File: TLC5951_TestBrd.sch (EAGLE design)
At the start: 7 parts, among them U1 V_REG_317SMD

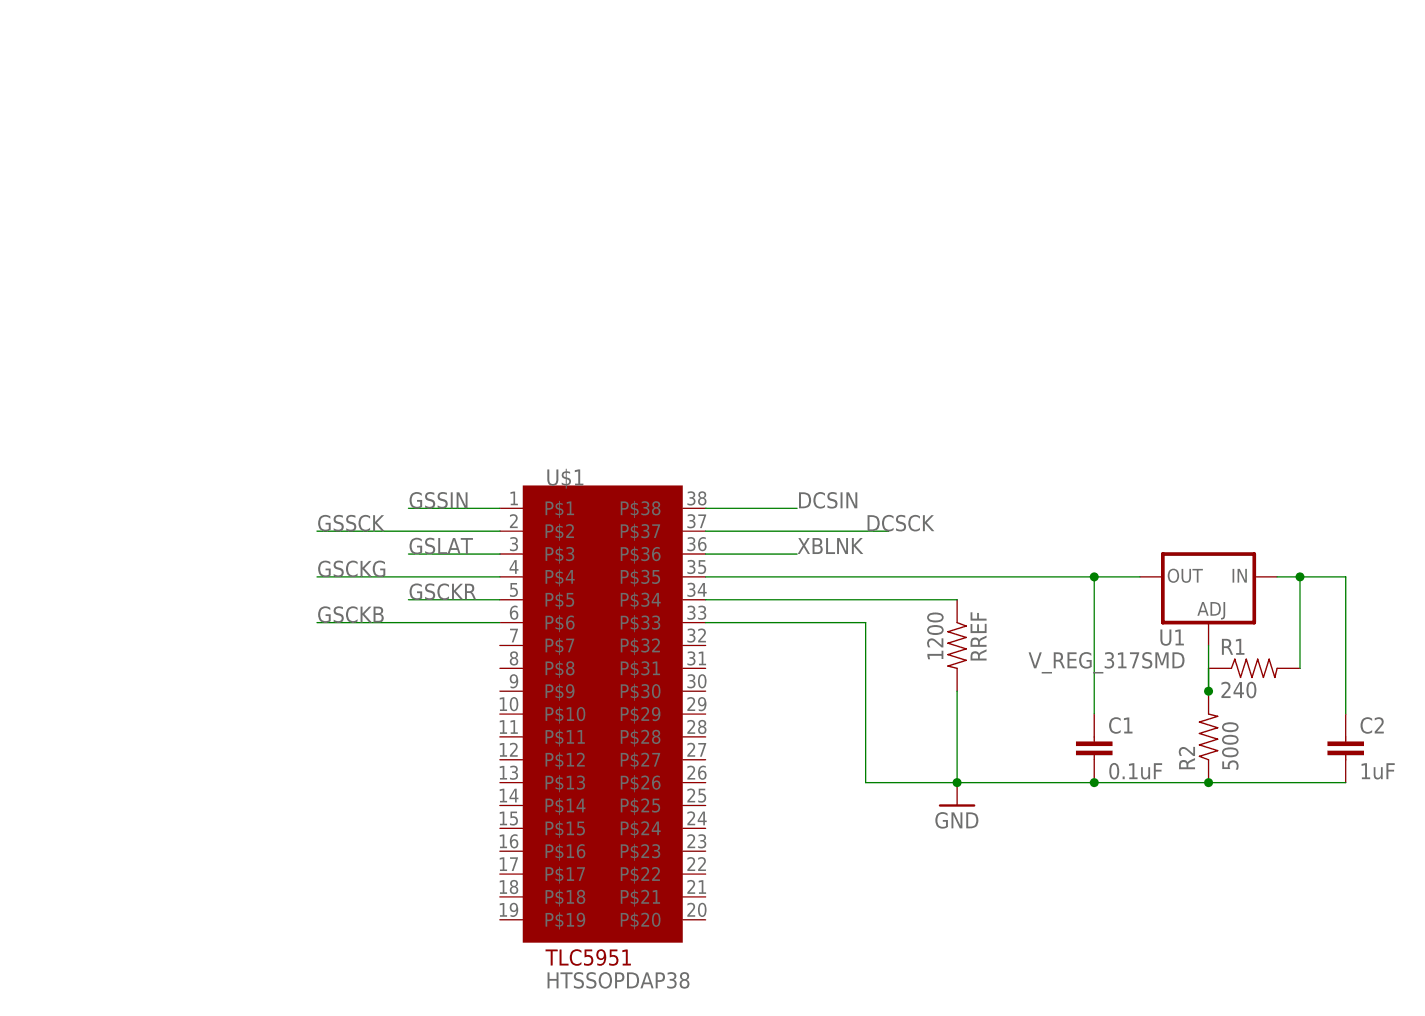
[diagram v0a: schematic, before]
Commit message: added new LDO Voltage Regulator
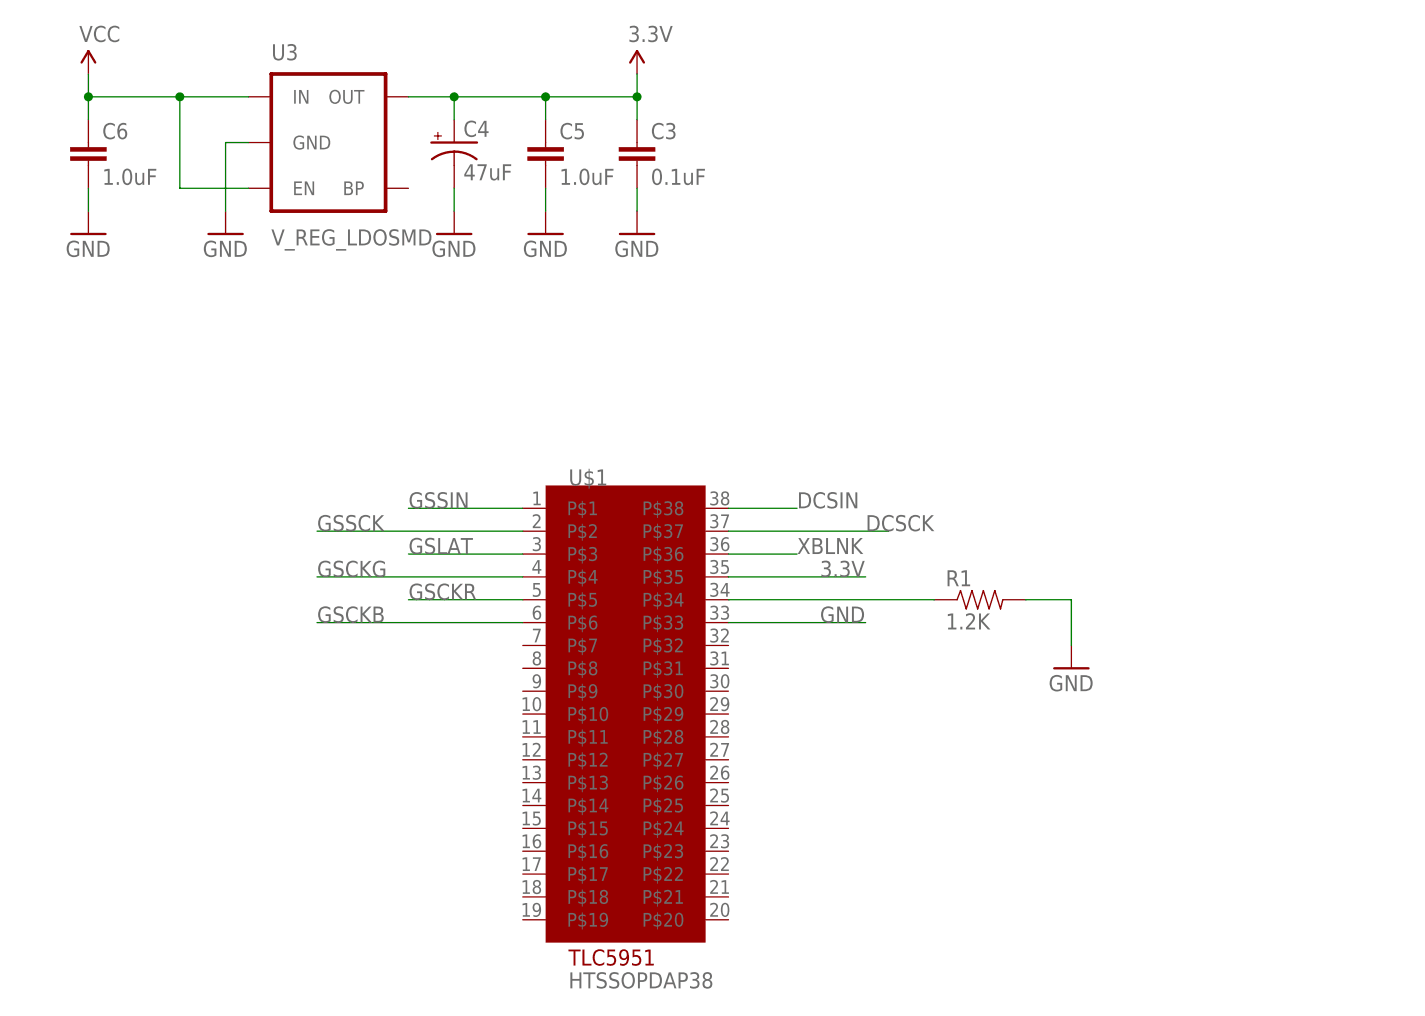
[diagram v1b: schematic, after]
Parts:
- removed C1: 0.1uF, SparkFun-Passives:CAP1210
- removed C2: 1uF, SparkFun-Passives:CAP1210
- removed R2: 5000, SparkFun-Passives:RESISTOR2512
- removed RREF: 1200, SparkFun-Passives:RESISTOR2512
- removed U1: V_REG_317SMD, SparkFun-PowerIC:V_REG_317SMD
- added C3: 0.1uF, SparkFun:CAP0402-CAP
- added C4: 47uF, SparkFun:CAP_POL3528
- added C5, C6: 1.0uF, SparkFun:CAP0402-CAP
- added U3: V_REG_LDOSMD, SparkFun:V_REG_LDOSMD
- R1: value 240 -> 1.2K; device SparkFun-Passives:RESISTOR2512 -> SparkFun-Passives:RESISTORPTH-1W
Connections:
- removed net N$1: RREF.1, U$1.P$34
- removed net N$3: C2.1, R1.2, U1.IN
- removed net N$4: R1.1, R2.2, U1.ADJ
- new net 3.3V: C3.1, C4.+, C5.1, U$1.P$35, U3.OUT
- new net VCC: C6.1, U3.EN, U3.IN
- net GND: now also C3.2, C4.-, C5.2, C6.2, R1.2, U3.GND; no longer C1.2, C2.2, R2.1, RREF.2
- net N$2: now also R1.1, U$1.P$34; no longer C1.1, U$1.P$35, U1.OUT
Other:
- moved on the sheet: R1, U$1

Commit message: Updated TLC5951 Eagle library and Breakout Board Project File
1. Updated TLC5951_DAP38 Eagle library by removing tsop under the
central section of the chip, and by adding holes.
2. Updated TLC5951_TestBrd schematic by adding headers and using new
DAP38 device details
3. Created TLC5951 layout with passive components and appropriate
traces.
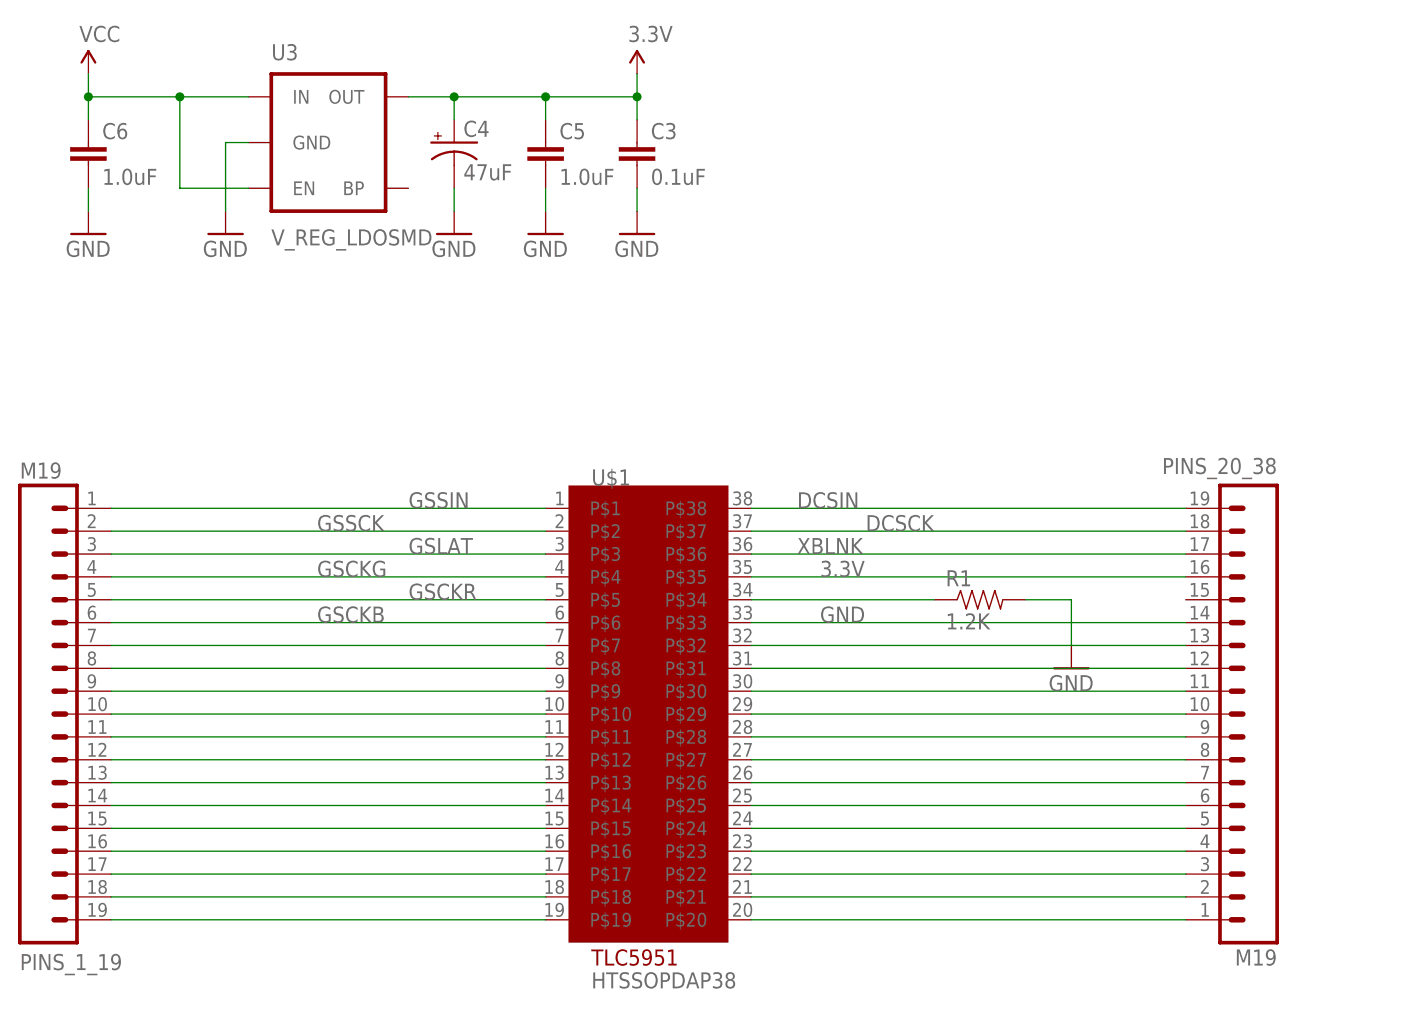
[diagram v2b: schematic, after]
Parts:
- added PINS_1_19, PINS_20_38: M19, SparkFun-Connectors:M19
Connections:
- new net N$1: PINS_20_38.13, U$1.P$32
- new net N$10: PINS_20_38.5, U$1.P$24
- new net N$11: PINS_20_38.4, U$1.P$23
- new net N$12: PINS_20_38.3, U$1.P$22
- new net N$13: PINS_20_38.2, U$1.P$21
- new net N$14: PINS_20_38.1, U$1.P$20
- new net N$15: PINS_1_19.7, U$1.P$7
- new net N$16: PINS_1_19.8, U$1.P$8
- new net N$17: PINS_1_19.9, U$1.P$9
- new net N$18: PINS_1_19.10, U$1.P$10
- new net N$19: PINS_1_19.11, U$1.P$11
- new net N$20: PINS_1_19.12, U$1.P$12
- new net N$21: PINS_1_19.13, U$1.P$13
- new net N$22: PINS_1_19.14, U$1.P$14
- new net N$23: PINS_1_19.15, U$1.P$15
- new net N$24: PINS_1_19.16, U$1.P$16
- new net N$25: PINS_1_19.17, U$1.P$17
- new net N$26: PINS_1_19.18, U$1.P$18
- new net N$27: PINS_1_19.19, U$1.P$19
- new net N$3: PINS_20_38.12, U$1.P$31
- new net N$4: PINS_20_38.11, U$1.P$30
- new net N$5: PINS_20_38.10, U$1.P$29
- new net N$6: PINS_20_38.9, U$1.P$28
- new net N$7: PINS_20_38.8, U$1.P$27
- new net N$8: PINS_20_38.7, U$1.P$26
- new net N$9: PINS_20_38.6, U$1.P$25
- net 3.3V: now also PINS_20_38.16
- net DCSCK: now also PINS_20_38.18
- net DCSIN: now also PINS_20_38.19
- net GND: now also PINS_20_38.14
- net GSCKB: now also PINS_1_19.6
- net GSCKG: now also PINS_1_19.4
- net GSCKR: now also PINS_1_19.5
- net GSLAT: now also PINS_1_19.3
- net GSSCK: now also PINS_1_19.2
- net GSSIN: now also PINS_1_19.1
- net XBLNK: now also PINS_20_38.17
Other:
- moved on the sheet: U$1
